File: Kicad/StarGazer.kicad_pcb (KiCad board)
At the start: 4 copper layers, 100 x 100 mm, 95 parts, among them J201 USB_B_Micro, J202 Conn_02x01 BATTERY, J301 I2C_CONNECTOR_OUT, J302 I2C_CONNECTOR_OUT, J303 SWD_DEBUG, J304 CONN_JOYSTICK, SW201 SW_DIP_x01, SW301 RESET PUSH, U101 STM32F070F6Px, U201 STBC08, U202 AP22811BW5, U203 TLV75528PDBV, U301 TSX-3225, U302 LIS3MDLTR, U303 LSM6DS33TR, U304 74HC595PW, U305 74HC595PW, U306 74HC595PW

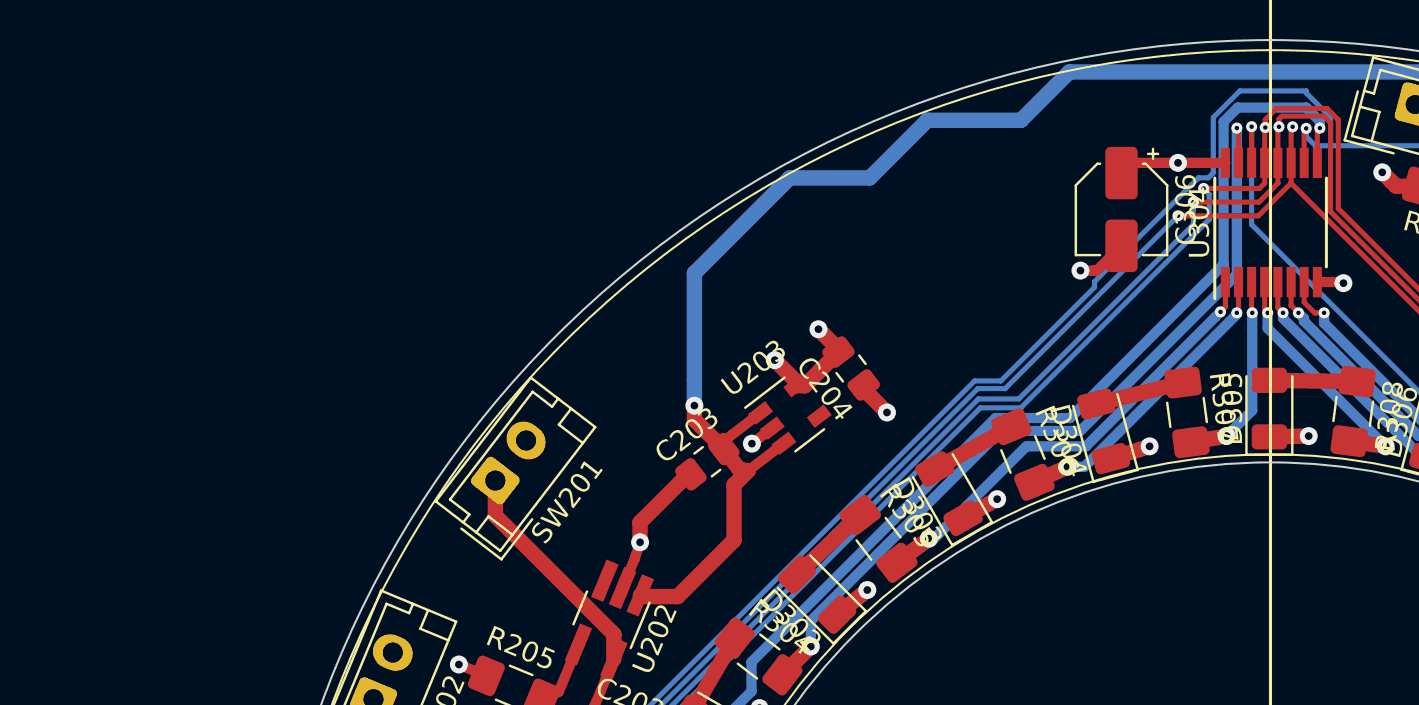
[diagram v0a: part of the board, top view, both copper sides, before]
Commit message: Calculating ram needed and current selected chip will not fit it.  Upgrading to a more capable chip.
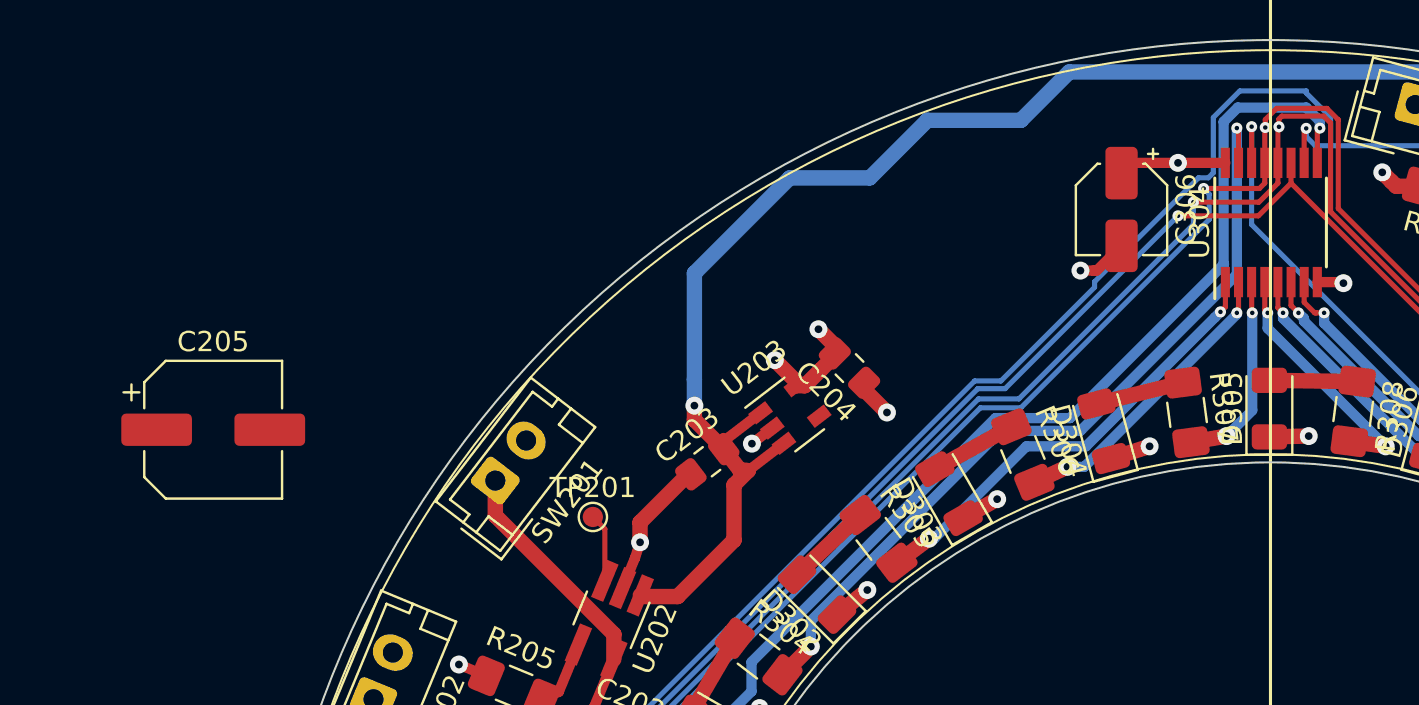
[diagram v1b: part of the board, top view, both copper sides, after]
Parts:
- added C205: 100uF, Capacitor_SMD:CP_Elec_6.3x5.2, F.Cu at (-52.3, -30.7)
- added TP201: TestPoint, TestPoint:TestPoint_Pad_D1.0mm, F.Cu at (-33.5, -26.4)
- C204: value 1uF -> 2.2uF
- D201: value LED -> Red
- D202: value LED -> Green
- D301, D302, D303, D304, D305, D306, D307, D308, D309, D310, D311, D312, D313, D314, D315, D316, D317, D318, D319, D320, D321, D322, D323, D324: value RING_LED -> Green
- J202: value Conn_02x01 BATTERY -> JST - 2x1
- J301, J302: value I2C_CONNECTOR_OUT -> JST - 4x1
- J303: value SWD_DEBUG -> JST - 5x1
- J304: value CONN_JOYSTICK -> JST - 5x1
- R101, R102, R201, R204, R205, R301: value 10k -> 10kohm
- R202, R203, R304, R305, R306, R307, R308, R309, R310, R311, R312, R313, R314, R315, R316, R317, R318, R319, R320, R321, R322, R323, R324, R325, R326, R327: value 330 -> 180ohm
- RV301: value R_POT -> Pot - 10kohm
- SW201: value SW_DIP_x01 -> JST - 2x1
- U101: value STM32F070F6Px -> STM32F070F6P6TR
- U202: value AP22811BW5 -> AP22811BW5-7
- U203: value TLV75528PDBV -> TLV75528PDBVR
- U304, U305, U306: value 74HC595PW -> 74HC595PW,112
- moved C204 0.08 mm to (-20.8, -33.8), turned to 135 degrees
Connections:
- U202 pad 3: (no net) -> Net-(TP201-Pad1)
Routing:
- net Net-(TP201-Pad1): track 0.00 -> 3.40 mm
- net SHIFT_REG_CLK: track 226.7 -> 224.9 mm, vias 4 -> 3

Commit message: Upgraded to STM32G0 for increased memory. Schematic and PCB are updated.  PCB now has radial grid applied in preparation of final part placement.
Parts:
- added D101: Green, Diode_SMD:D_1206_3216Metric, F.Cu at (199.1, 86.5)
- added D102: Red, Diode_SMD:D_1206_3216Metric, F.Cu at (201.8, 85.8)
- added R103: 180ohm, Resistor_SMD:R_1206_3216Metric_Pad1.42x1.75mm_HandSolder, F.Cu at (200.5, 80.7)
- added TP101: Connector_TestPoint, TestPoint:TestPoint_Pad_D1.0mm, F.Cu at (193.2, 75.3)
- added TP102: Connector_TestPoint, TestPoint:TestPoint_Pad_D1.0mm, F.Cu at (193.8, 77.5)
- R102: value 10kohm -> 180ohm
- U101: value STM32F070F6P6TR -> STM32G070KBT6; footprint Package_SO:TSSOP-20_4.4x6.5mm_P0.65mm -> Package_QFP:LQFP-32_7x7mm_P0.8mm
- moved C205 202.1 mm to (131.4, 53.6), turned to 315 degrees
- moved R102 194.2 mm to (197.7, 81.4), turned to 285 degrees
- moved C305 187.7 mm to (176.2, 128.0), turned to 112.5 degrees
- moved U101 183.1 mm to (199.5, 72.3), turned to 285 degrees
- moved C204 183.0 mm to (144.2, 45.4), turned to 127.5 degrees
- moved U303 182.8 mm to (176.1, 123.5), turned to 112.5 degrees
- moved U203 182.6 mm to (141.0, 47.3), turned to 30 degrees
- moved C203 182.1 mm to (136.6, 49.1), turned to 30 degrees
- moved C102 182.0 mm to (197.1, 63.5), turned to 195 degrees
- moved J304 180.7 mm to (206.0, 80.9)
- moved C201 180.2 mm to (113.6, 91.8)
- moved C202 180.2 mm to (126.4, 69.5)
- moved C301 180.2 mm to (191.3, 53.6)
- moved C302 180.2 mm to (170.3, 46.6)
- moved C303 180.2 mm to (183.7, 48.1)
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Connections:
- J301 pad 2: I2C_SDA -> I2C_SCL
- J301 pad 3: I2C_SCL -> I2C_SDA
- J302 pad 2: I2C_SDA -> I2C_SCL
- J302 pad 3: I2C_SCL -> I2C_SDA
- J304 pad 2: UI_BUTTON -> UI_JOY_Y
- J304 pad 4: UI_JOY_Y -> UI_BUTTON
- R101 pad 1: GND -> SWCLK
- R101 pad 2: Net-(R101-Pad2) -> GND
- R102 pad 1: GND -> Net-(R102-Pad1)
- R102 pad 2: Net-(R102-Pad2) -> Net-(D101-Pad2)
- R302 pad 2: I2C_SDA -> I2C_SCL
- R303 pad 2: I2C_SCL -> I2C_SDA
- U101 pad 1: Net-(R101-Pad2) -> (no net)
- U101 pad 10: Net-(R102-Pad2) -> SHIFT_REG_OUTPUT_ENABLE_N
- U101 pad 11: SHIFT_REG_CLK -> SHIFT_REG_LATCH
- U101 pad 12: GND -> (no net)
- U101 pad 13: SHIFT_REG_DATA_IN -> (no net)
- U101 pad 14: UI_BUTTON -> (no net)
- U101 pad 15: GND -> Net-(TP101-Pad1)
- U101 pad 16: V_REG -> Net-(TP102-Pad1)
- U101 pad 17: I2C_SCL -> Net-(R102-Pad1)
- U101 pad 18: I2C_SDA -> Net-(R103-Pad1)
- U101 pad 19: SWDIO -> (no net)
- U101 pad 20: SWCLK -> (no net)
- U101 pad 4: RESET_N -> V_REG
- U101 pad 5: V_REG -> GND
- U101 pad 6: UI_JOY_X -> RESET_N
- U101 pad 7: UI_JOY_Y -> (no net)
- U101 pad 8: SHIFT_REG_OUTPUT_ENABLE_N -> SHIFT_REG_CLK
- U101 pad 9: SHIFT_REG_LATCH -> SHIFT_REG_DATA_IN
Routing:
- net UI_JOY_Y: track 31.8 -> 9.07 mm, vias 1 -> 0
- net I2C_SCL: track 128.7 -> 149.9 mm
- net UI_JOY_X: track 26.7 -> 11.7 mm, vias 1 -> 0
- net I2C_SDA: track 126.8 -> 141.6 mm
- net SWCLK: track 48.7 -> 57.6 mm, vias 1 -> 3
- net SHIFT_REG_DATA_IN: track 58.4 -> 51.8 mm
- net SWDIO: track 52.6 -> 57.4 mm, vias 1 -> 3
- net OSC_IN: track 18.9 -> 23.0 mm
- net Net-(R102-Pad1): track 0.00 -> 3.25 mm
- net SHIFT_REG_OUTPUT_ENABLE_N: track 229.7 -> 232.9 mm
- net Net-(R103-Pad1): track 0.00 -> 3.07 mm
- net Net-(TP102-Pad1): track 0.00 -> 3.06 mm
- net Net-(TP101-Pad1): track 0.00 -> 3.03 mm
- net Net-(R101-Pad2): track 3.01 -> 0.00 mm
- net Net-(R102-Pad2): track 3.00 -> 0.00 mm
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
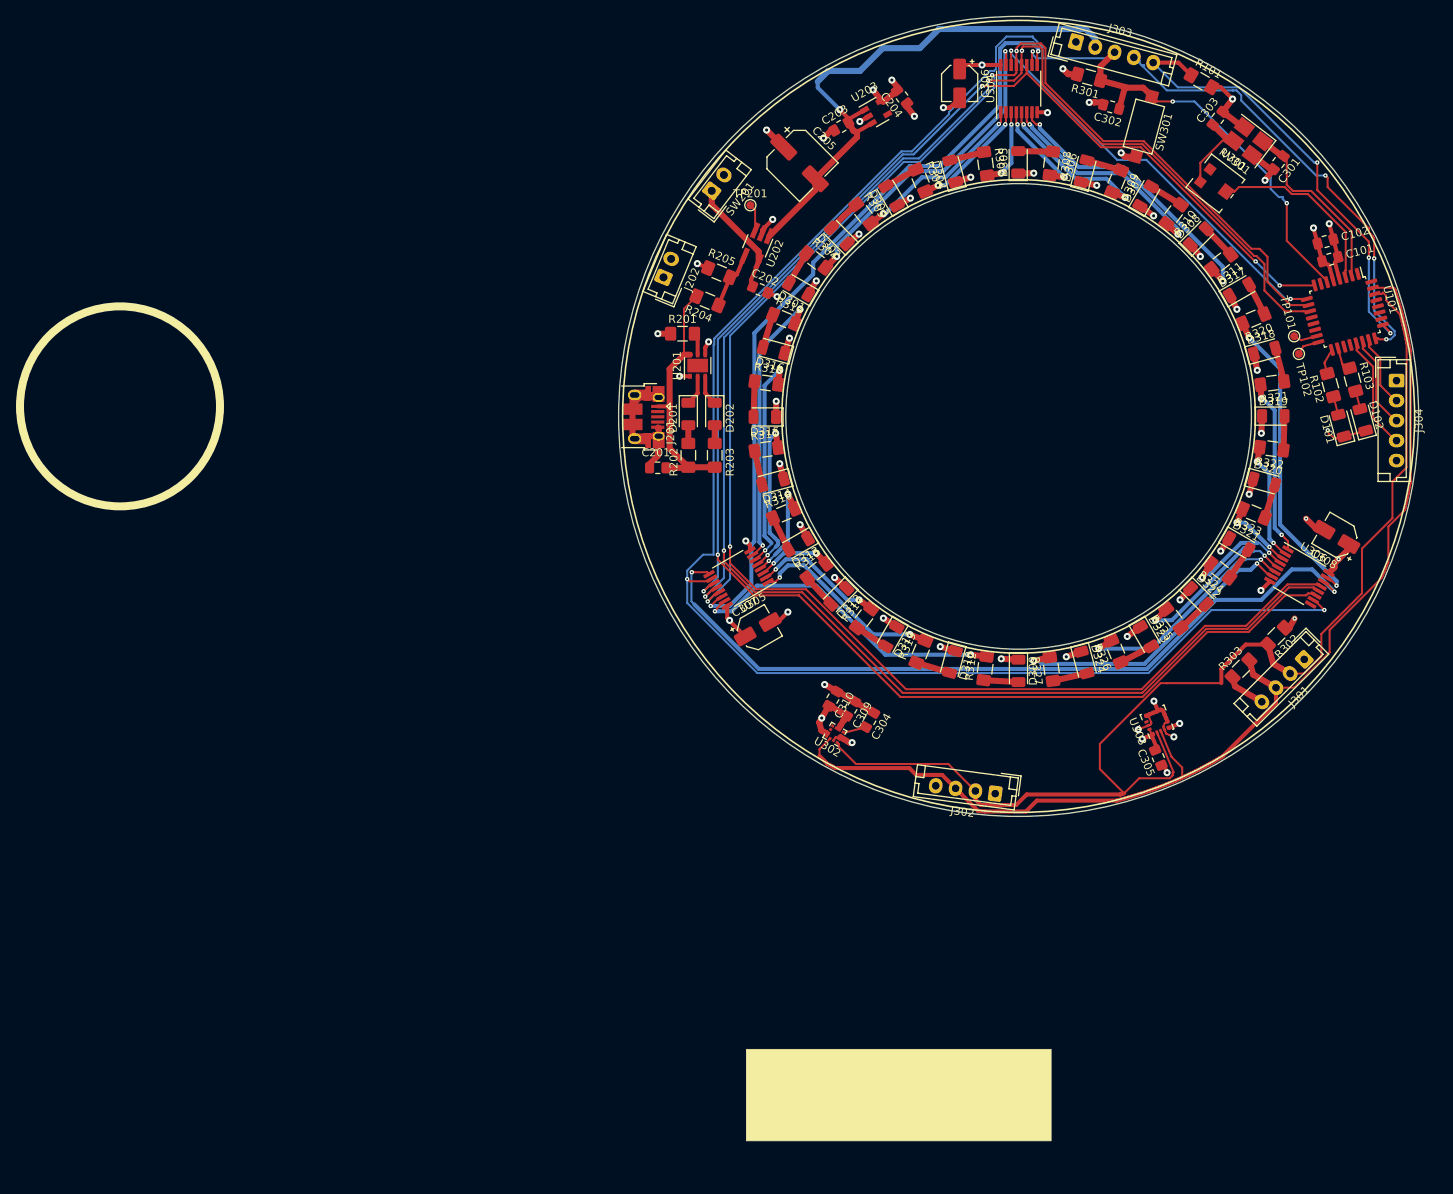
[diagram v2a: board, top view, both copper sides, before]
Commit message: Shift register tracing remade to curved.  Hand hurty
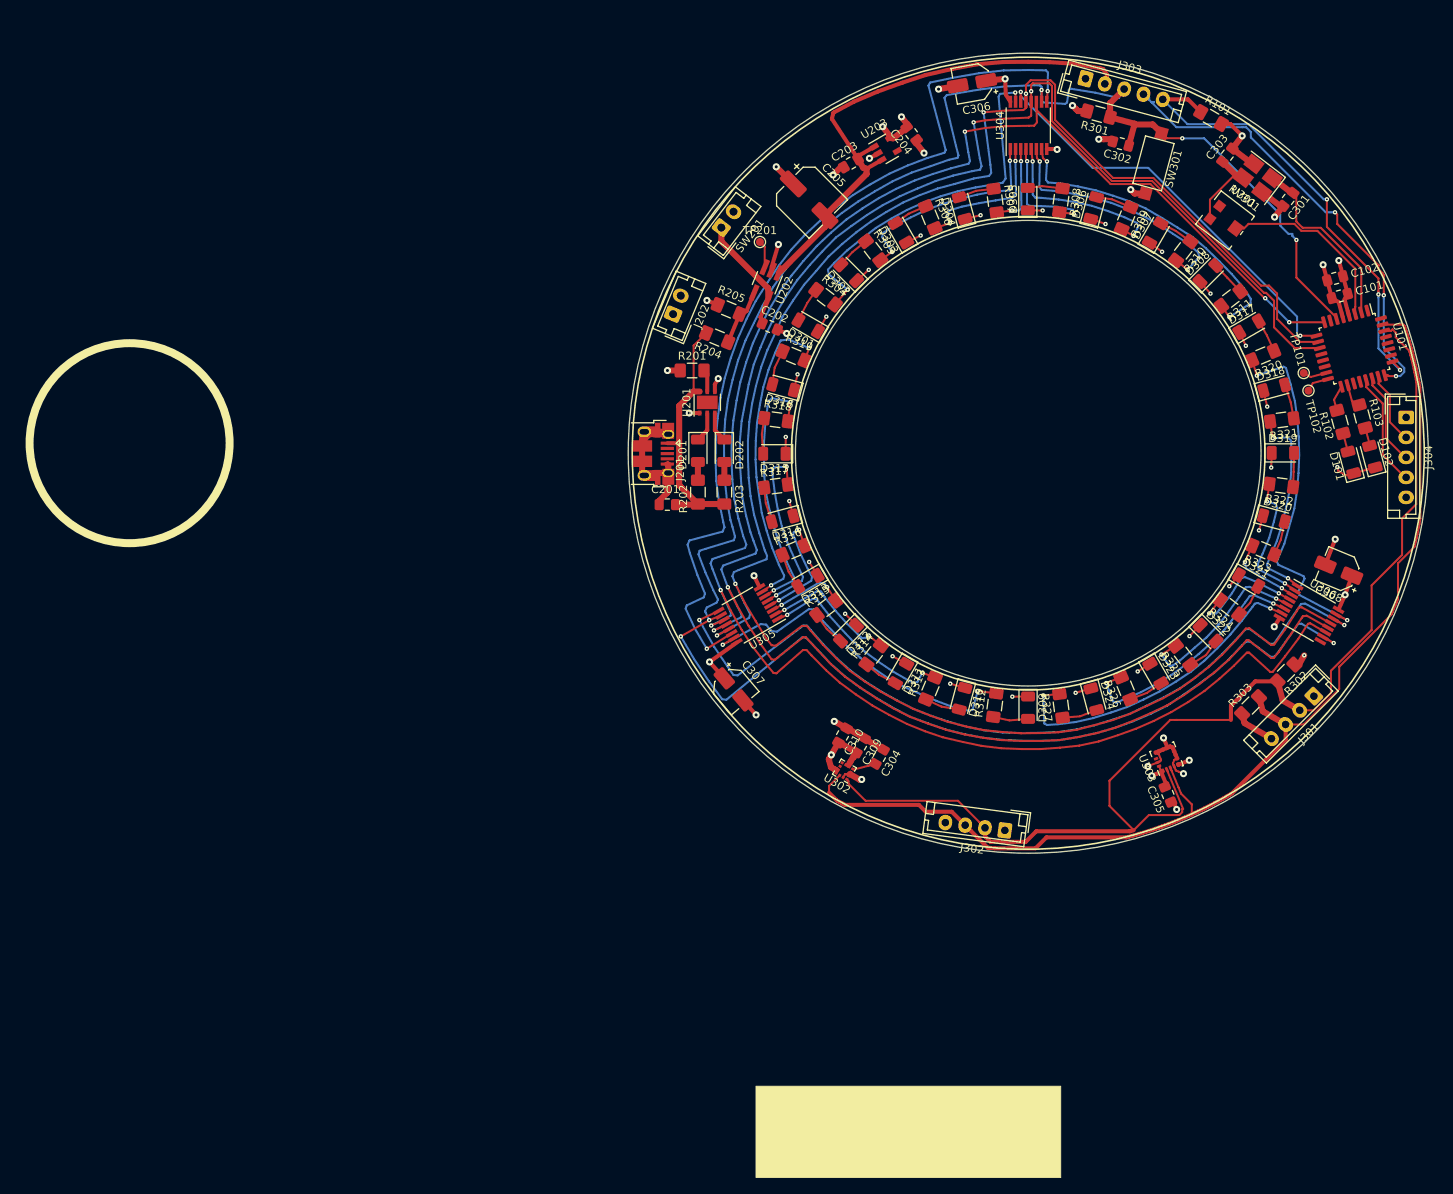
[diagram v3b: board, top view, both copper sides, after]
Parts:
- moved C307 8.09 mm to (123.1, 119.5), turned to 310.2 degrees
- moved C309 4.75 mm to (139.0, 126.4)
- moved D101 4.75 mm to (200.3, 91.1)
- moved D317 4.75 mm to (187.6, 74.1)
- moved D321 4.75 mm to (187.5, 105.9)
- moved R327 4.75 mm to (164.1, 121.5)
- moved U306 4.75 mm to (195.0, 110.0)
- moved D201 4.75 mm to (118.7, 89.6)
- moved D202 4.75 mm to (122.0, 89.6)
- moved D315 4.75 mm to (128.2, 90.0)
- moved J201 4.75 mm to (113.1, 90.0)
- moved J202 4.75 mm to (115.6, 72.5)
- moved R204 4.75 mm to (121.1, 75.5)
- moved R318 4.75 mm to (128.4, 85.7)
- moved U202 4.75 mm to (127.2, 68.6)
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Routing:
- net RESET_N: track 249.7 -> 268.8 mm, vias 5 -> 6
- net Net-(U304-Pad9): track 97.6 -> 112.4 mm
- net SHIFT_REG_CLK: track 222.3 -> 236.7 mm
- net SHIFT_REG_LATCH: track 232.4 -> 244.5 mm
- net SHIFT_REG_OUTPUT_ENABLE_N: track 232.9 -> 243.3 mm
- net Net-(R320-Pad2): track 39.2 -> 45.5 mm
- net Net-(R318-Pad2): track 27.5 -> 32.5 mm
- net Net-(R304-Pad2): track 40.4 -> 45.4 mm
- net Net-(U305-Pad9): track 97.9 -> 102.9 mm
- net Net-(R305-Pad2): track 22.6 -> 26.7 mm
- net Net-(R319-Pad2): track 35.5 -> 39.4 mm
- net Net-(R317-Pad2): track 20.0 -> 23.8 mm
- net Net-(R311-Pad2): track 36.5 -> 40.2 mm
- net Net-(R321-Pad2): track 22.1 -> 25.4 mm
- net Net-(R312-Pad2): track 40.7 -> 43.9 mm
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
